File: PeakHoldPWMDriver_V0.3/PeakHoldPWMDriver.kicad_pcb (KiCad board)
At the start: 2 copper layers, 100.1 x 50 mm, 117 parts, among them J1 RND 205-00203, J2 RND 205-00205, Q1 2N7002, Q10 2N7002, Q11 2N7002, Q12 2N7002, Q13 TSM2309, Q14 IRLL 024N, Q15 TSM2309, Q16 IRLL 024N, Q17 TSM2309, Q18 TSM2309, Q19 TSM2309, Q2 2N7002, Q20 TSM2309, Q3 2N7002, Q4 2N7002, Q5 TSM2309, Q6 TSM2309, Q7 IRLL 024N, Q8 IRLL 024N, Q9 2N7002, U1 74LS32, U2 LM2901, U3 74LS74, U4 LTC6992, U5 74LS74, U6 LM340, U7 74LS08, U8 74LS08

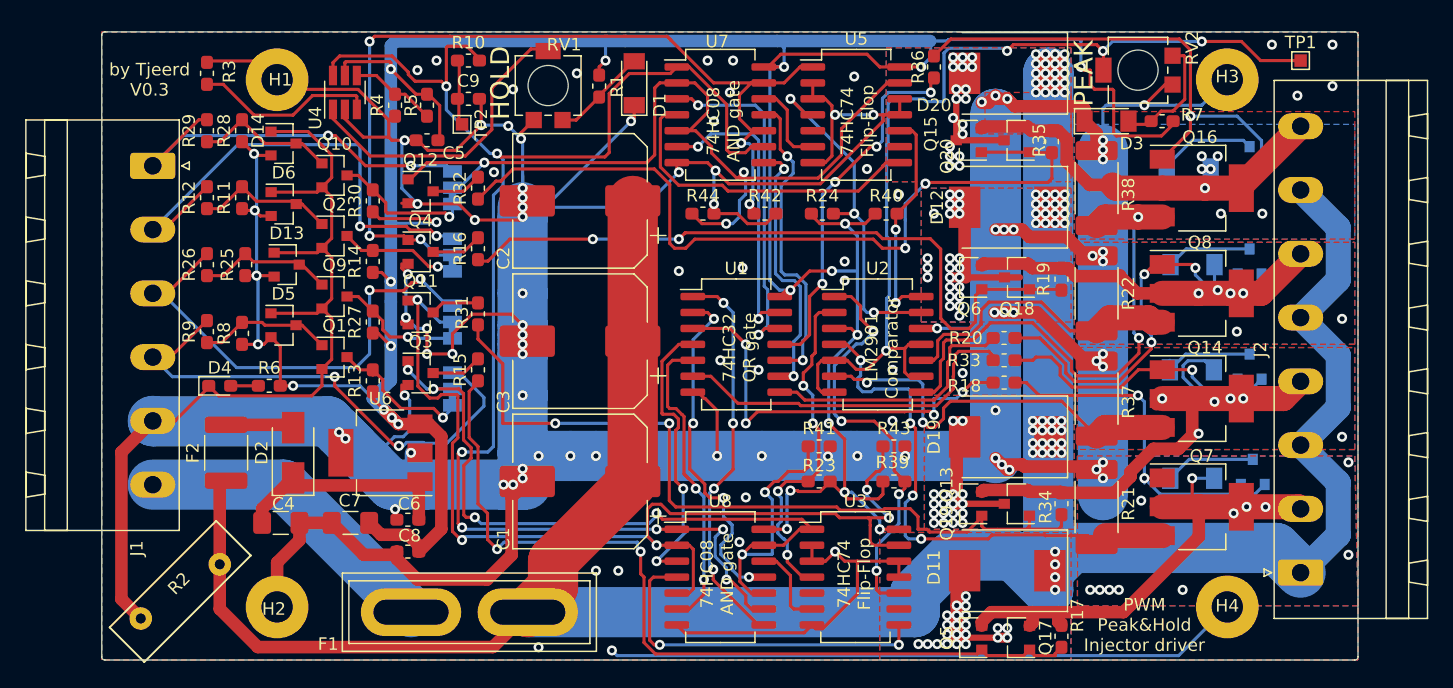
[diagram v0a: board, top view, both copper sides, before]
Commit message: PCB and schematic updated with battery voltage compensation
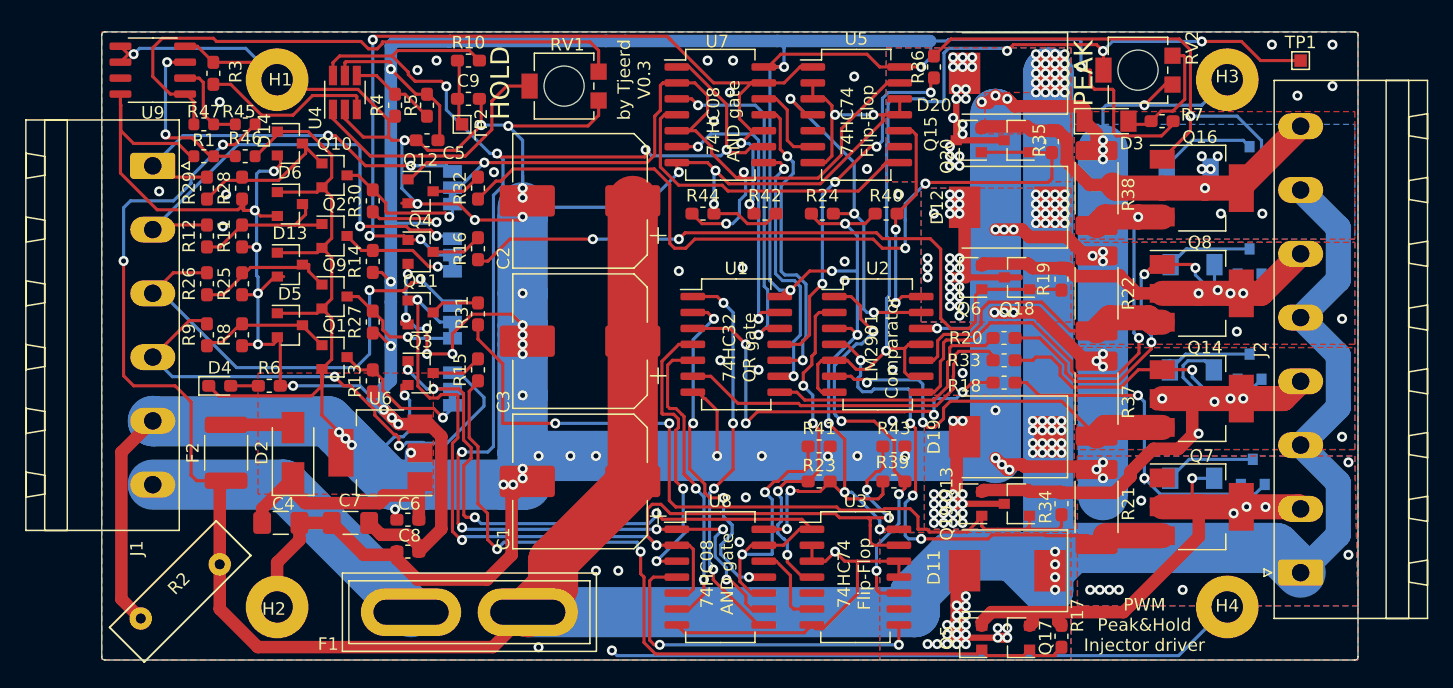
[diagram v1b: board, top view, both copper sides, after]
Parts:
- removed D1: BAV103, Diode_SMD:D_MiniMELF
- added R45: 91k, Resistor_SMD:R_0603_1608Metric, F.Cu at (123.2, 73.4)
- added R46: 9.1k, Resistor_SMD:R_0603_1608Metric, F.Cu at (123.2, 75.9)
- added R47: 6.2k, Resistor_SMD:R_0603_1608Metric, F.Cu at (119.9, 73.4)
- added U9: LM2904, Package_SO:SO-8_3.9x4.9mm_P1.27mm, F.Cu at (115.8, 69.1)
- R1: value 470R -> 15k; footprint Resistor_SMD:R_0603_1608Metric_Pad1.05x0.95mm_HandSolder -> Resistor_SMD:R_0603_1608Metric
- moved R1 32.0 mm to (119.9, 75.9), turned to 180 degrees
- moved R28 4.57 mm to (122.9, 78.5)
- moved R29 4.57 mm to (120.1, 78.5)
- moved R11 3.05 mm to (122.9, 82.3)
- moved R12 3.05 mm to (120.1, 82.3)
- moved R25 1.55 mm to (122.9, 86.1)
- moved R26 1.52 mm to (120.1, 86.1)
- moved RV1 1.27 mm to (148.6, 70.4), turned to 270 degrees
- moved R3 0.51 mm to (120.7, 69.3)
- moved D14 0.51 mm to (126.7, 74.9)
- moved D5 0.51 mm to (126.7, 89.4)
- moved D6 0.49 mm to (126.7, 79.8)
- moved R9 0.25 mm to (120.1, 90.2)
- moved D13 0.25 mm to (126.7, 84.6)
- moved R8 0.11 mm to (122.9, 90.2)
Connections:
- R1 pad 1: 5V -> Net-(R1-Pad1)
- R1 pad 2: Net-(D1-Pad2) -> 5V
- RV1 pad 3: Net-(D1-Pad2) -> Net-(R47-Pad2)
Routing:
- net Net-(R47-Pad2): track 0.00 -> 46.7 mm
- net VBAT: track 219.1 -> 261.3 mm, vias 56 -> 58
- net 5V: track 291.6 -> 319.2 mm
- net Net-(R1-Pad1): track 0.00 -> 13.8 mm, vias 0 -> 2
- net PWR_GND: track 605.0 -> 617.6 mm, vias 103 -> 104
- net Net-(D1-Pad2): track 7.60 -> 0.00 mm
- net Net-(R45-Pad2): track 0.00 -> 7.26 mm
- net Net-(RV1-Pad2): track 24.5 -> 21.3 mm
- net Net-(C4-Pad2): track 18.2 -> 19.7 mm
- net INJ4: track 31.9 -> 30.7 mm
- net Net-(D14-Pad3): track 11.4 -> 12.4 mm
- net INJ2: track 38.8 -> 38.1 mm
- net PWM: track 120.5 -> 121.1 mm, vias 7 -> 9
- net Net-(R3-Pad1): track 14.7 -> 14.2 mm
- net Net-(D11-Pad2): vias 22 -> 20
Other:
- rule trace_min: 0.2 -> 0.25

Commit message: Changed resistor value R5, now correct PWM freqency
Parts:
- R11, R25, R28, R41, R43, R44, R8: value 1K -> 10K
- R12, R26, R29, R9: value 1K -> 470R
